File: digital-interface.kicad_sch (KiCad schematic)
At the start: 13 parts, among them U32001 Si8641BD-B-IS2, U32002 R05C05TE05S

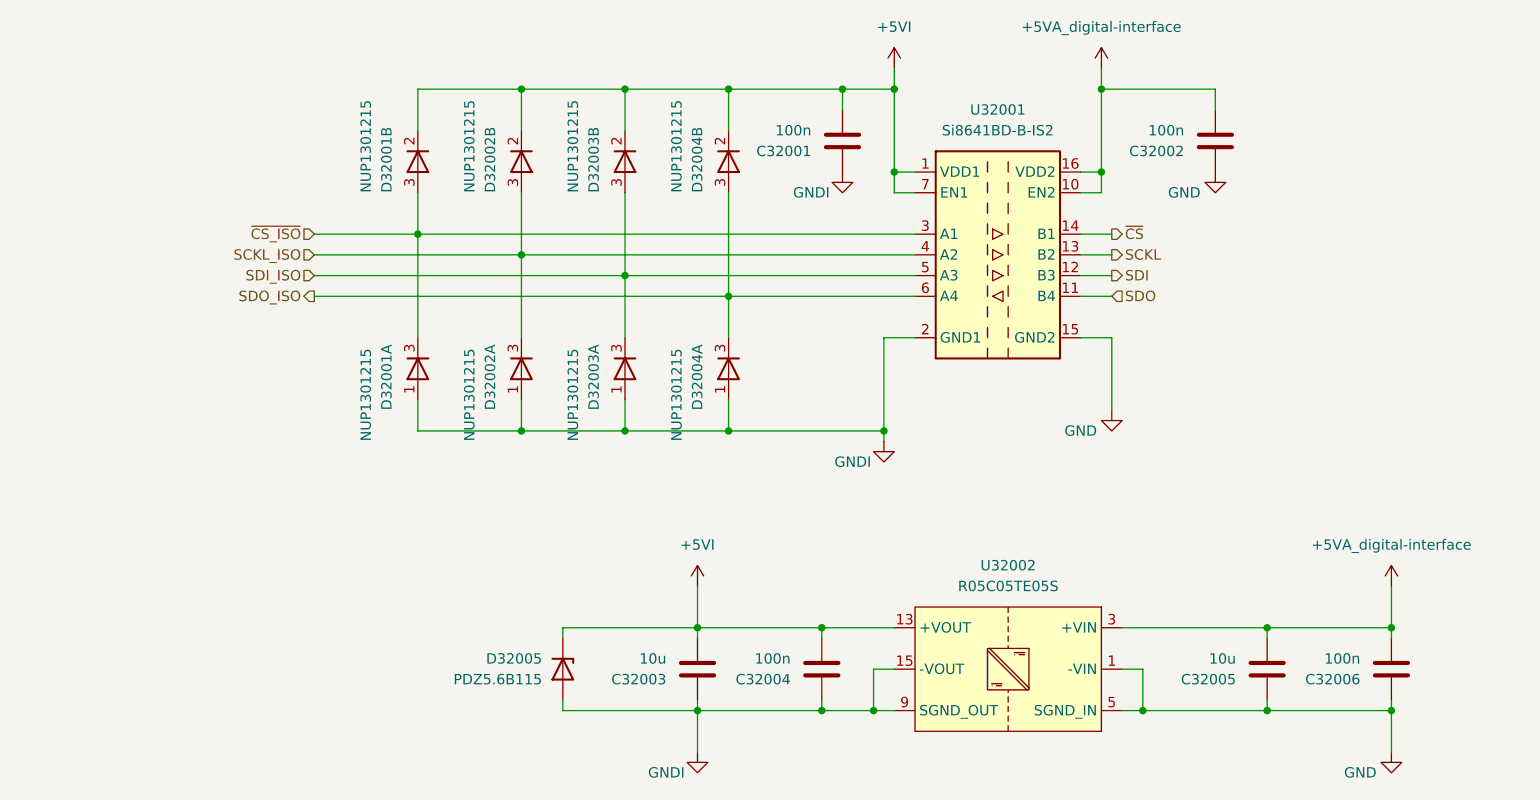
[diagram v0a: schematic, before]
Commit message: add pss 3dmodels and testpoints
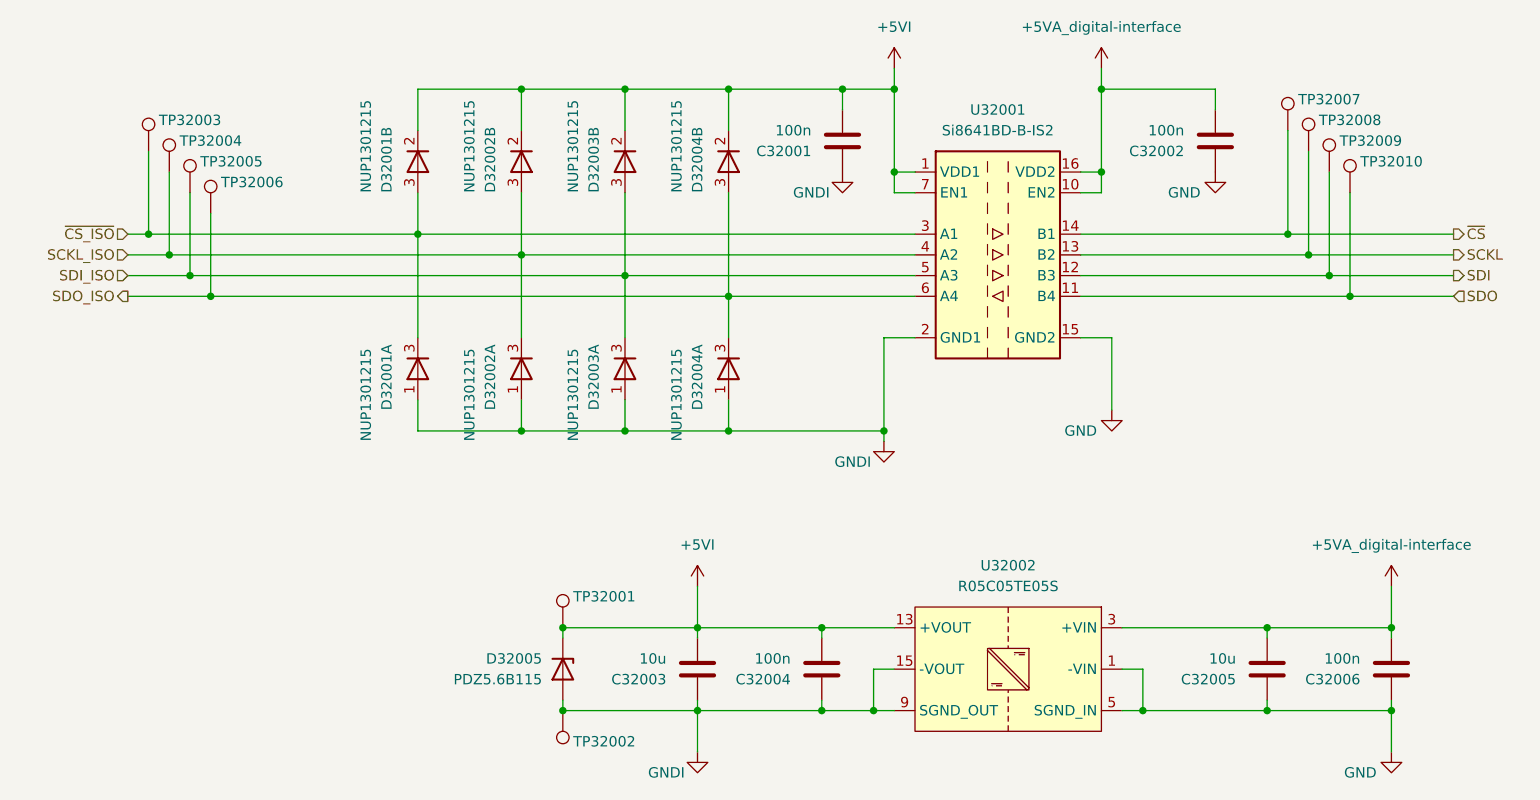
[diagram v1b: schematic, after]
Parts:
- added TP32001, TP32002, TP32003, TP32004, TP32005, TP32006, TP32007, TP32008, TP32009, TP32010: ~, pss:TP_0805_2012Metric, symbol Connector:TestPoint
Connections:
- net +5VI: now also TP32001.1
- net GNDI: now also TP32002.1
- net SCKL: now also TP32008.1
- net SCKL_ISO: now also TP32004.1
- net SDI: now also TP32009.1
- net SDI_ISO: now also TP32005.1
- net SDO: now also TP32010.1
- net SDO_ISO: now also TP32006.1
- net ~{CS_ISO}: now also TP32003.1
- net ~{CS}: now also TP32007.1

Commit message: edit pss symbol library: export all schematic symbols to library 'pss' and update symbol link
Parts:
- D32001, D32002, D32003, D32004: symbol Device:D_Dual_Series_AKC_Split -> pss:D_Dual_Series_AKC_Split
- D32005: symbol Device:D_Zener -> pss:D_Zener
- TP32001, TP32002, TP32003, TP32004, TP32005, TP32006, TP32007, TP32008, TP32009, TP32010: symbol Connector:TestPoint -> pss:TestPoint
- U32001: symbol Isolator:Si8641BD-B-IS2 -> pss:Si8641BD-B-IS2
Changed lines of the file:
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@@
 	)
 	(symbol
-		(lib_id "Connector:TestPoint")
+		(lib_id "pss:TestPoint")
 		(at 48.26 63.5 0)
 		(unit 1)
@@
 	)
 	(symbol
-		(lib_id "Device:D_Dual_Series_AKC_Split")
+		(lib_id "pss:D_Dual_Series_AKC_Split")
 		(at 114.3 85.09 90)
 		(unit 1)
@@
 	)
 	(symbol
-		(lib_id "Connector:TestPoint")
+		(lib_id "pss:TestPoint")
 		(at 185.42 58.42 0)
 		(unit 1)
@@
 	)
 	(symbol
-		(lib_id "Connector:TestPoint")
+		(lib_id "pss:TestPoint")
 		(at 43.18 58.42 0)
 		(unit 1)
@@
 	)
 	(symbol
-		(lib_id "Device:D_Dual_Series_AKC_Split")
+		(lib_id "pss:D_Dual_Series_AKC_Split")
 		(at 76.2 59.69 270)
 		(unit 2)
@@
 	)
 	(symbol
-		(lib_id "Device:D_Dual_Series_AKC_Split")
+		(lib_id "pss:D_Dual_Series_AKC_Split")
 		(at 88.9 59.69 270)
 		(unit 2)
@@
 	)
 	(symbol
-		(lib_id "Device:D_Dual_Series_AKC_Split")
+		(lib_id "pss:D_Dual_Series_AKC_Split")
 		(at 114.3 59.69 270)
 		(unit 2)
@@
 	)
 	(symbol
-		(lib_id "Connector:TestPoint")
+		(lib_id "pss:TestPoint")
 		(at 190.5 63.5 0)
 		(unit 1)
@@
 	)
 	(symbol
-		(lib_id "Device:D_Zener")
+		(lib_id "pss:D_Zener")
 		(at 93.98 121.92 270)
 		(unit 1)
@@
 	)
 	(symbol
-		(lib_id "Connector:TestPoint")
+		(lib_id "pss:TestPoint")
 		(at 50.8 66.04 0)
 		(unit 1)
@@
 	)
 	(symbol
-		(lib_id "Connector:TestPoint")
+		(lib_id "pss:TestPoint")
 		(at 187.96 60.96 0)
 		(unit 1)
@@
 	)
 	(symbol
-		(lib_id "Device:D_Dual_Series_AKC_Split")
+		(lib_id "pss:D_Dual_Series_AKC_Split")
 		(at 88.9 85.09 90)
 		(unit 1)
@@
 	)
 	(symbol
-		(lib_id "Device:D_Dual_Series_AKC_Split")
+		(lib_id "pss:D_Dual_Series_AKC_Split")
 		(at 101.6 85.09 90)
 		(unit 1)
@@
 	)
 	(symbol
-		(lib_id "Connector:TestPoint")
+		(lib_id "pss:TestPoint")
 		(at 93.98 116.84 0)
 		(unit 1)
@@
 	)
 	(symbol
-		(lib_id "Connector:TestPoint")
+		(lib_id "pss:TestPoint")
 		(at 45.72 60.96 0)
 		(unit 1)
@@
 	)
 	(symbol
-		(lib_id "Connector:TestPoint")
+		(lib_id "pss:TestPoint")
 		(at 182.88 55.88 0)
 		(unit 1)
@@
 	)
 	(symbol
-		(lib_id "Connector:TestPoint")
+		(lib_id "pss:TestPoint")
 		(at 93.98 127 0)
 		(mirror x)
@@
 	)
 	(symbol
-		(lib_id "Device:D_Dual_Series_AKC_Split")
+		(lib_id "pss:D_Dual_Series_AKC_Split")
 		(at 76.2 85.09 90)
 		(unit 1)
@@
 	)
 	(symbol
-		(lib_id "Device:D_Dual_Series_AKC_Split")
+		(lib_id "pss:D_Dual_Series_AKC_Split")
 		(at 101.6 59.69 270)
 		(unit 2)
@@
 	)
 	(symbol
-		(lib_id "Isolator:Si8641BD-B-IS2")
+		(lib_id "pss:Si8641BD-B-IS2")
 		(at 147.32 71.12 0)
 		(unit 1)
